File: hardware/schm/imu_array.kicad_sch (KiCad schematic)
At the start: 16 parts, among them U3 MCP23S17T-E/SS, U4 LSM6DSV320XTR, U5 H3LIS331DLTR, U6 H3LIS331DLTR

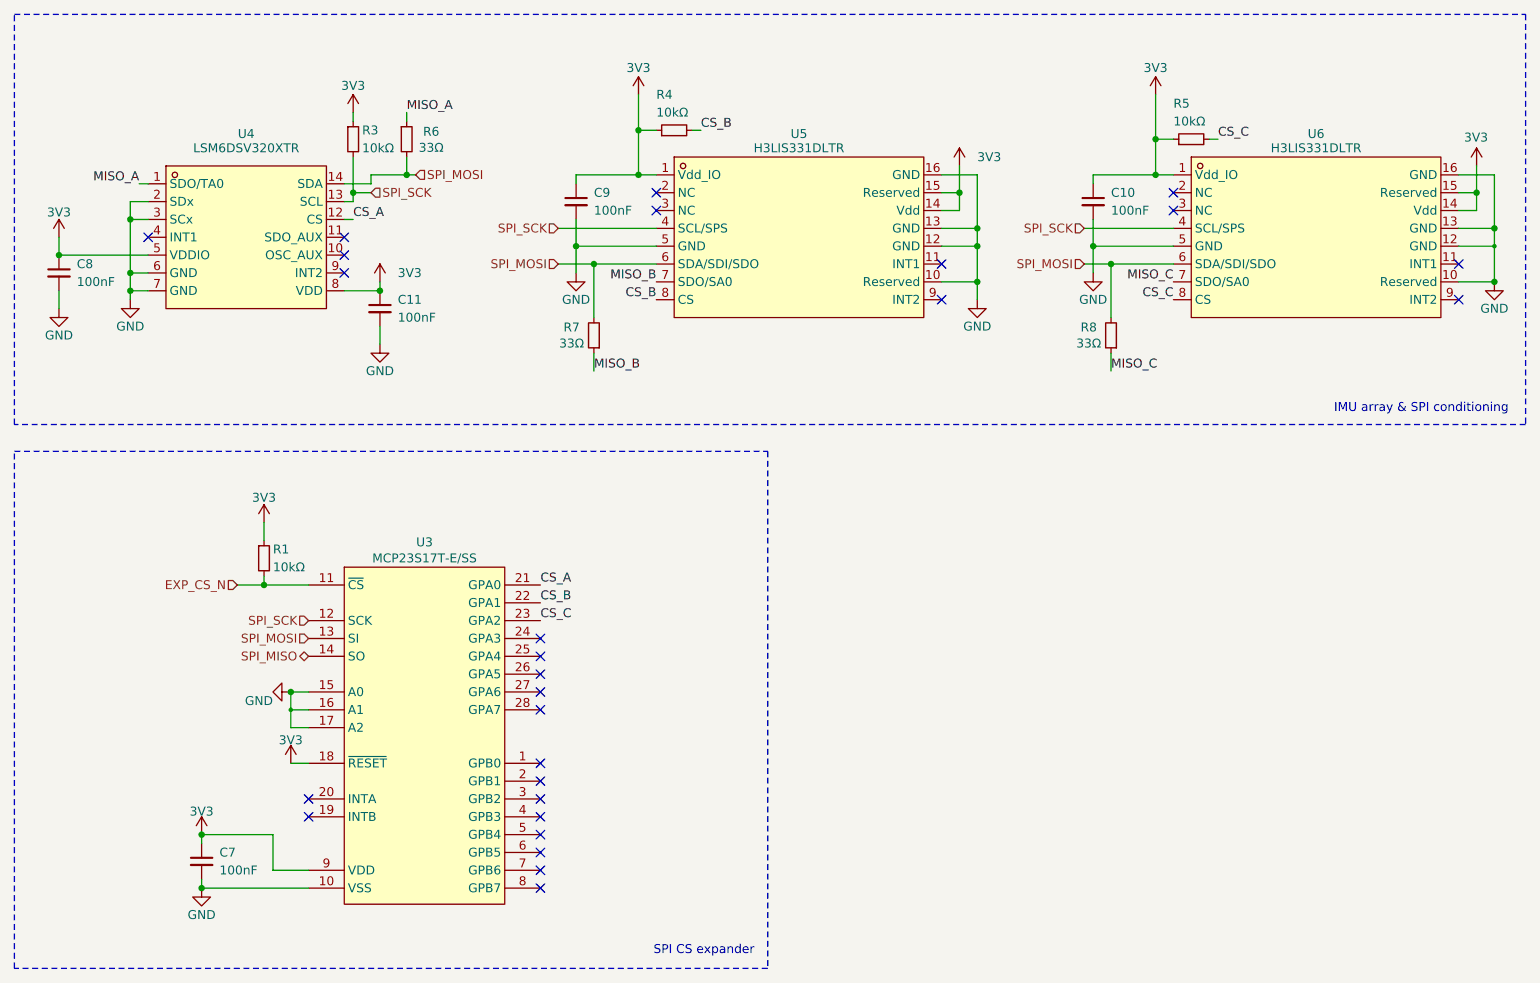
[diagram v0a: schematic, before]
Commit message: feat: swap to the 74HC595 for cs expansion
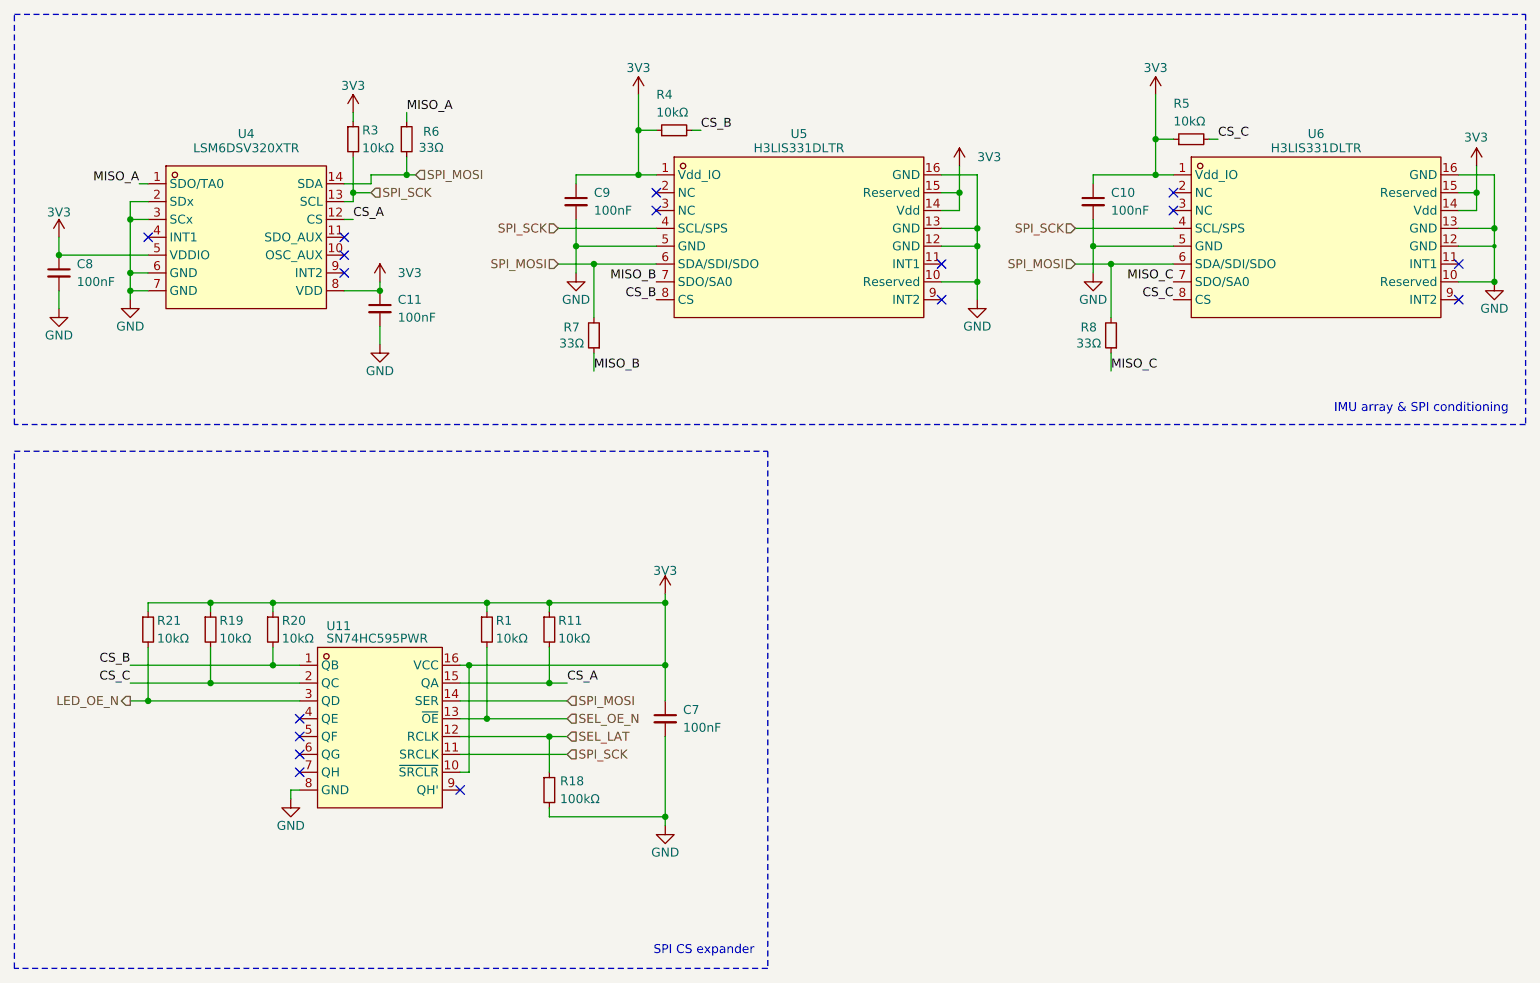
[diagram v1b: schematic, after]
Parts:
- removed U3: MCP23S17T-E/SS, Library:SSOP-28_L10.2-W5.3-P0.65-LS7.8-BL, symbol Library:MCP23S17T-E_SS
- added R11, R19, R20, R21: 10kΩ, Resistor_SMD:R_0402_1005Metric, symbol Device:R_Small
- added R18: 100kΩ, Resistor_SMD:R_0402_1005Metric, symbol Device:R_Small
- added U11: SN74HC595PWR, Device:TSSOP-16_L5.0-W4.4-P0.65-LS6.4-BL, symbol Device:SN74HC595PWR
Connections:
- net 3V3: now also R11.1, R19.1, R20.1, R21.1, U11.10 (~{SRCLR}), U11.16 (VCC)
- net CS_A: now also R11.2, U11.15 (QA)
- net CS_B: now also R20.2, U11.1 (QB)
- net CS_C: now also R19.2, U11.2 (QC)
- net GND: now also R18.2, U11.8 (GND)
- net SPI_MOSI: now also U11.14 (SER)
- net SPI_SCK: now also U11.11 (SRCLK)
- net EXP_CS_N renamed SEL_OE_N
- net SEL_OE_N: now also U11.13 (~{OE})
- new net LED_OE_N: R21.2, U11.3 (QD)
- new net SEL_LAT: R18.1, U11.12 (RCLK)
- no-connect marks 27 -> 17
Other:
- moved on the sheet: C7, R1

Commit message: feat: add bom placement
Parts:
- C10, C11, C7, C8, C9: LCSC Part NONE -> C169834
- R1, R11, R19, R20, R21, R3, R4, R5: LCSC Part NONE -> C844715
- R18: LCSC Part NONE -> C2077080
- R6, R7, R8: LCSC Part NONE -> C3008986
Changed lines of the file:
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@@
 			)
 		)
-		(property "LCSC Part" "NONE"
+		(property "LCSC Part" "C844715"
 			(at 25.4 -91.44 0)
 			(hide yes)
@@
 			)
 		)
-		(property "LCSC Part" "NONE"
+		(property "LCSC Part" "C3008986"
 			(at -53.34 218.44 0)
 			(hide yes)
@@
 			)
 		)
-		(property "LCSC Part" "NONE"
+		(property "LCSC Part" "C844715"
 			(at -233.68 54.61 0)
 			(hide yes)
@@
 			)
 		)
-		(property "LCSC Part" "NONE"
+		(property "LCSC Part" "C844715"
 			(at -15.24 140.97 0)
 			(hide yes)
@@
 			)
 		)
-		(property "LCSC Part" "NONE"
+		(property "LCSC Part" "C844715"
 			(at -251.46 54.61 0)
 			(hide yes)
@@
 			)
 		)
-		(property "LCSC Part" "NONE"
+		(property "LCSC Part" "C3008986"
 			(at 222.25 -54.61 0)
 			(hide yes)
@@
 			)
 		)
-		(property "LCSC Part" "NONE"
+		(property "LCSC Part" "C2077080"
 			(at -194.31 77.47 0)
 			(hide yes)
@@
 			)
 		)
-		(property "LCSC Part" "NONE"
+		(property "LCSC Part" "C169834"
 			(at -2.54 -76.2 0)
 			(hide yes)
@@
 			)
 		)
-		(property "LCSC Part" "NONE"
+		(property "LCSC Part" "C844715"
 			(at -242.57 54.61 0)
 			(hide yes)
@@
 			)
 		)
-		(property "LCSC Part" "NONE"
+		(property "LCSC Part" "C169834"
 			(at -8.89 -66.04 0)
 			(hide yes)
@@
 			)
 		)
-		(property "LCSC Part" "NONE"
+		(property "LCSC Part" "C169834"
 			(at -170.18 82.55 0)
 			(hide yes)
@@
 			)
 		)
-		(property "LCSC Part" "NONE"
+		(property "LCSC Part" "C844715"
 			(at -194.31 54.61 0)
 			(hide yes)
@@
 			)
 		)
-		(property "LCSC Part" "NONE"
+		(property "LCSC Part" "C169834"
 			(at -6.35 -76.2 0)
 			(hide yes)
@@
 			)
 		)
-		(property "LCSC Part" "NONE"
+		(property "LCSC Part" "C844715"
 			(at -203.2 54.61 0)
 			(hide yes)
@@
 			)
 		)
-		(property "LCSC Part" "NONE"
+		(property "LCSC Part" "C844715"
 			(at 58.42 212.09 0)
 			(hide yes)
@@
 			)
 		)
-		(property "LCSC Part" "NONE"
+		(property "LCSC Part" "C169834"
 			(at 36.83 -218.12 0)
 			(hide yes)
@@
 			)
 		)
-		(property "LCSC Part" "NONE"
+		(property "LCSC Part" "C3008986"
 			(at 20.32 288.29 0)
 			(hide yes)

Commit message: feat: add pulldown resister and note mode 0
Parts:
- added R22: 100kΩ, Resistor_SMD:R_0402_1005Metric, symbol Device:R_Small
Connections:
- net GND: now also R22.2
- net SPI_SCK: now also R22.1
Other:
- note added: "SPI pulldown"
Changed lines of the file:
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@@
 		)
 	)
+	(rectangle
+		(start 126.365 77.47)
+		(end 230.505 117.475)
+		(stroke
+			(width 0.1)
+			(type dash)
+		)
+		(fill
+			(type none)
+		)
+	)
+	(text "SPI pulldown"
+		(exclude_from_sim no)
+		(at 229.616 116.078 0)
+		(effects
+			(font
+				(size 1.27 1.27)
+			)
+			(justify right bottom)
+		)
+	)
 	(text "SPI CS expander"
 		(exclude_from_sim no)
@@
 	(wire
 		(pts
+			(xy 146.05 96.52) (xy 146.05 91.44)
+		)
+		(stroke
+			(width 0)
+			(type default)
+		)
+	)
+	(wire
+		(pts
 			(xy 31.75 107.95) (xy 52.07 107.95)
 		)
@@
 	(wire
 		(pts
+			(xy 146.05 101.6) (xy 146.05 104.14)
+		)
+		(stroke
+			(width 0)
+			(type default)
+		)
+	)
+	(wire
+		(pts
 			(xy 67.31 54.61) (xy 62.23 54.61)
 		)
@@
 	(hierarchical_label "SPI_SCK"
 		(shape input)
+		(at 146.05 91.44 180)
+		(effects
+			(font
+				(size 1.27 1.27)
+			)
+			(justify right)
+		)
+	)
+	(hierarchical_label "SPI_SCK"
+		(shape input)
 		(at 93.98 120.65 0)
 		(effects
@@
 	)
 	(symbol
+		(lib_id "power:GND")
+		(at 146.05 104.14 0)
+		(unit 1)
+		(body_style 1)
+		(exclude_from_sim no)
+		(in_bom yes)
+		(on_board yes)
+		(in_pos_files yes)
+		(dnp no)
+		(fields_autoplaced yes)
+		(property "Reference" "#PWR030"
+			(at 146.05 106.68 0)
+			(hide yes)
+			(show_name no)
+			(do_not_autoplace no)
+			(effects
+				(font
+					(size 1.27 1.27)
+				)
+			)
+		)
+		(property "Value" "GND"
+			(at 146.05 107.95 0)
+			(show_name no)
+			(do_not_autoplace no)
+			(effects
+				(font
+					(size 1.27 1.27)
+				)
+			)
+		)
+		(property "Footprint" ""
+			(at 146.05 104.14 0)
+			(show_name no)
+			(do_not_autoplace no)
+			(effects
+				(font
+					(size 1.27 1.27)
+				)
+			)
+		)
+		(property "Datasheet" "~"
+			(at 146.05 104.14 0)
+			(hide yes)
+			(show_name no)
+			(do_not_autoplace no)
+			(effects
+				(font
+					(size 1.27 1.27)
+				)
+			)
+		)
+		(property "Description" ""
+			(at 146.05 104.14 0)
+			(show_name no)
+			(do_not_autoplace no)
+			(effects
+				(font
+					(size 1.27 1.27)
+				)
+			)
+		)
+		(pin "1"
+		)
+		(instances
+			(project "circuit"
+				(path "/5ff26309-9be7-4732-9683-b5a799424d79/9e7afb3e-f6d0-4714-a3a9-7f1e1c051738"
+					(reference "#PWR030")
+					(unit 1)
+				)
+			)
+		)
+	)
+	(symbol
 		(lib_id "Device:R_Small")
 		(at 97.79 60.96 180)
@@
 					(unit 1)
 				)
+			)
+		)
+	)
+	(symbol
+		(lib_id "Device:R_Small")
+		(at 146.05 99.06 0)
+		(unit 1)
+		(body_style 1)
+		(exclude_from_sim no)
+		(in_bom yes)
+		(on_board yes)
+		(in_pos_files yes)
+		(dnp no)
+		(property "Reference" "R22"
+			(at 147.574 97.79 0)
+			(show_name no)
+			(do_not_autoplace no)
+			(effects
+				(font
+					(size 1.27 1.27)
+				)
+				(justify left)
+			)
+		)
+		(property "Value" "100kΩ"
+			(at 147.574 100.33 0)
+			(show_name no)
+			(do_not_autoplace no)
+			(effects
+				(font
+					(size 1.27 1.27)
+				)
+				(justify left)
+			)
+		)
+		(property "Footprint" "Resistor_SMD:R_0402_1005Metric"
+			(at 146.05 99.06 0)
+			(hide yes)
+			(show_name no)
+			(do_not_autoplace no)
+			(effects
+				(font
+					(size 1.27 1.27)
+				)
+			)
+		)
+		(property "Datasheet" "~"
+			(at 146.05 99.06 0)
+			(hide yes)
+			(show_name no)
+			(do_not_autoplace no)
+			(effects
+				(font
+					(size 1.27 1.27)
+				)
+			)
+		)
+		(property "Description" ""
+			(at 146.05 99.06 0)
+			(show_name no)
+			(do_not_autoplace no)
+			(effects
+				(font
+					(size 1.27 1.27)
+				)
+			)
+		)
+		(property "LCSC Part" "C2077080"
+			(at -139.7 50.8 0)
+			(hide yes)
+			(show_name no)
+			(do_not_autoplace no)
+			(effects
+				(font
+					(size 1.27 1.27)
+				)
+			)
+		)
+		(pin "1"
+		)
+		(pin "2"
+		)
+		(instances
+			(project "circuit"
+				(path "/5ff26309-9be7-4732-9683-b5a799424d79/9e7afb3e-f6d0-4714-a3a9-7f1e1c051738"
+					(reference "R22")
+					(unit 1)
+				)

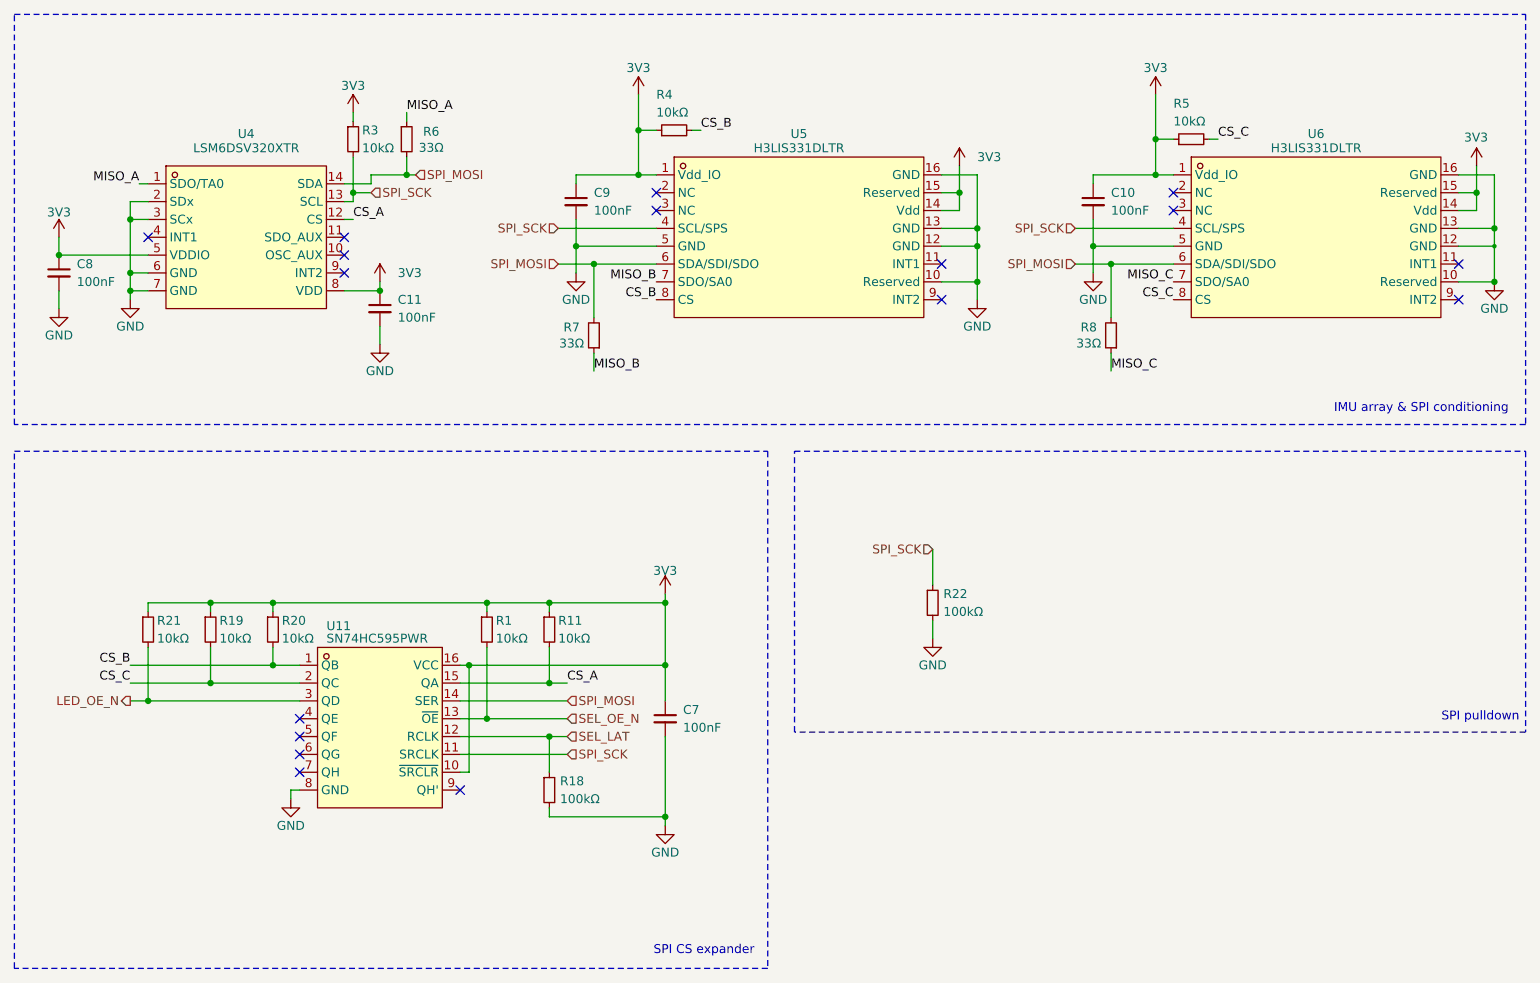
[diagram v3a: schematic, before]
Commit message: feat: review from tyler + align circuit.py
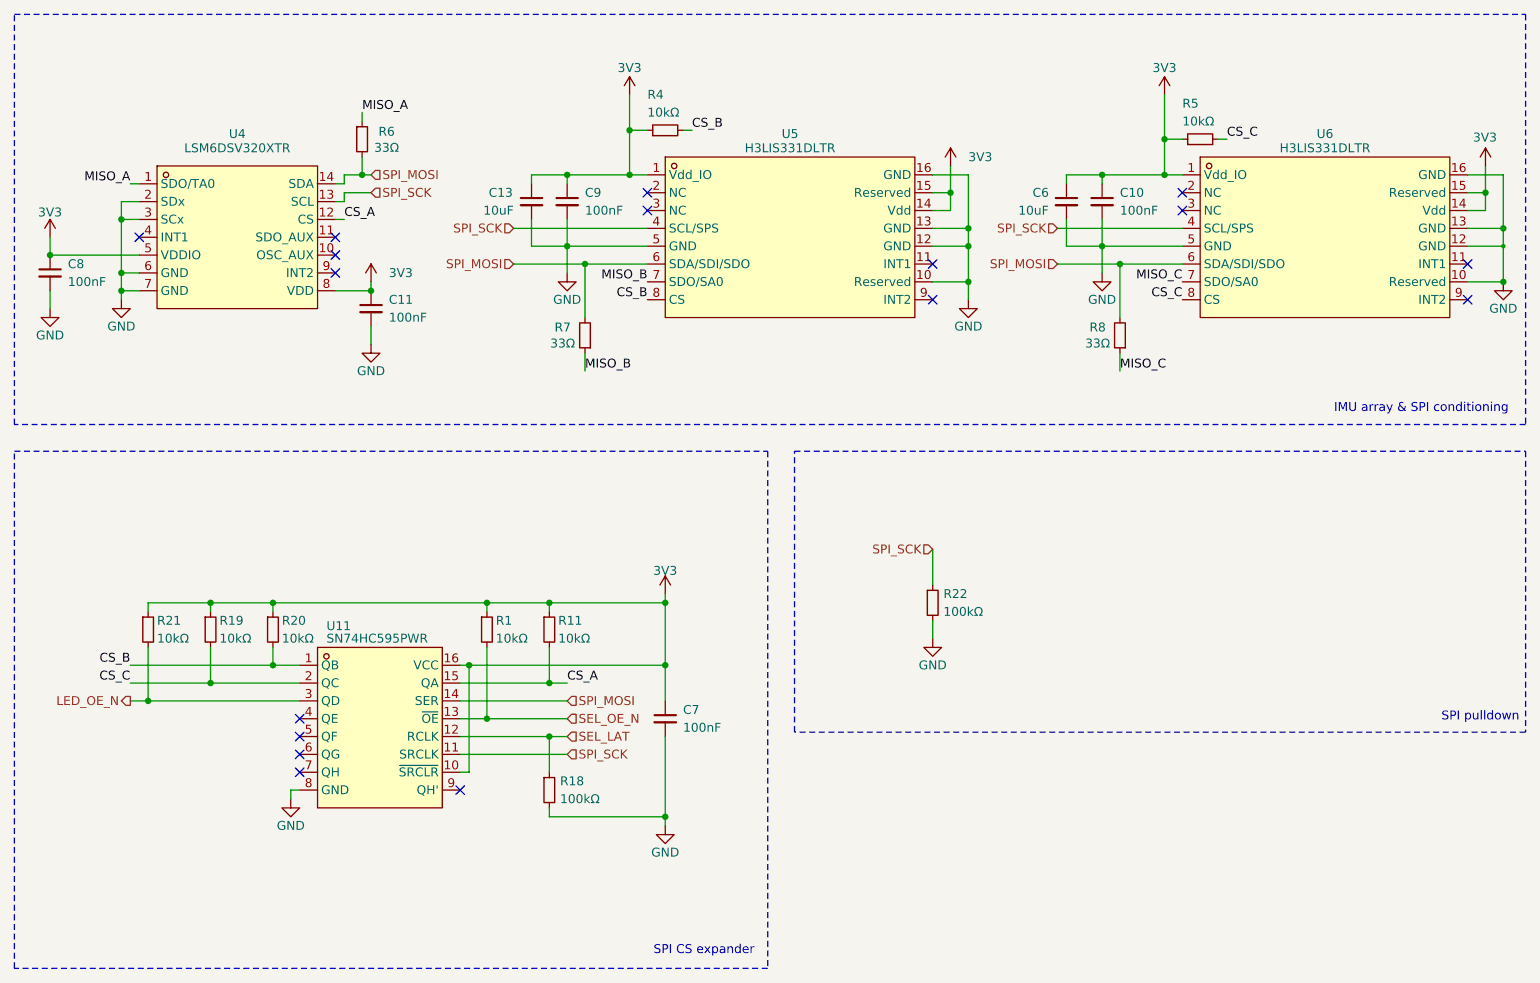
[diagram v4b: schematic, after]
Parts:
- removed R3: 10kΩ, Resistor_SMD:R_0402_1005Metric, symbol Device:R_Small
- added C13, C6: 10uF, Capacitor_SMD:C_0603_1608Metric, symbol Device:C_Small
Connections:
- net 3V3: now also C13.1, C6.1
- net GND: now also C13.2, C6.2
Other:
- moved on the sheet: C10, C11, C8, C9, R4, R5, R6, R7, R8, U4, U5, U6
